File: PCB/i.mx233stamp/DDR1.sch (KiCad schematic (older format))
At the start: 19 parts, among them U2 MT46V32M16TG, U3 M25P32

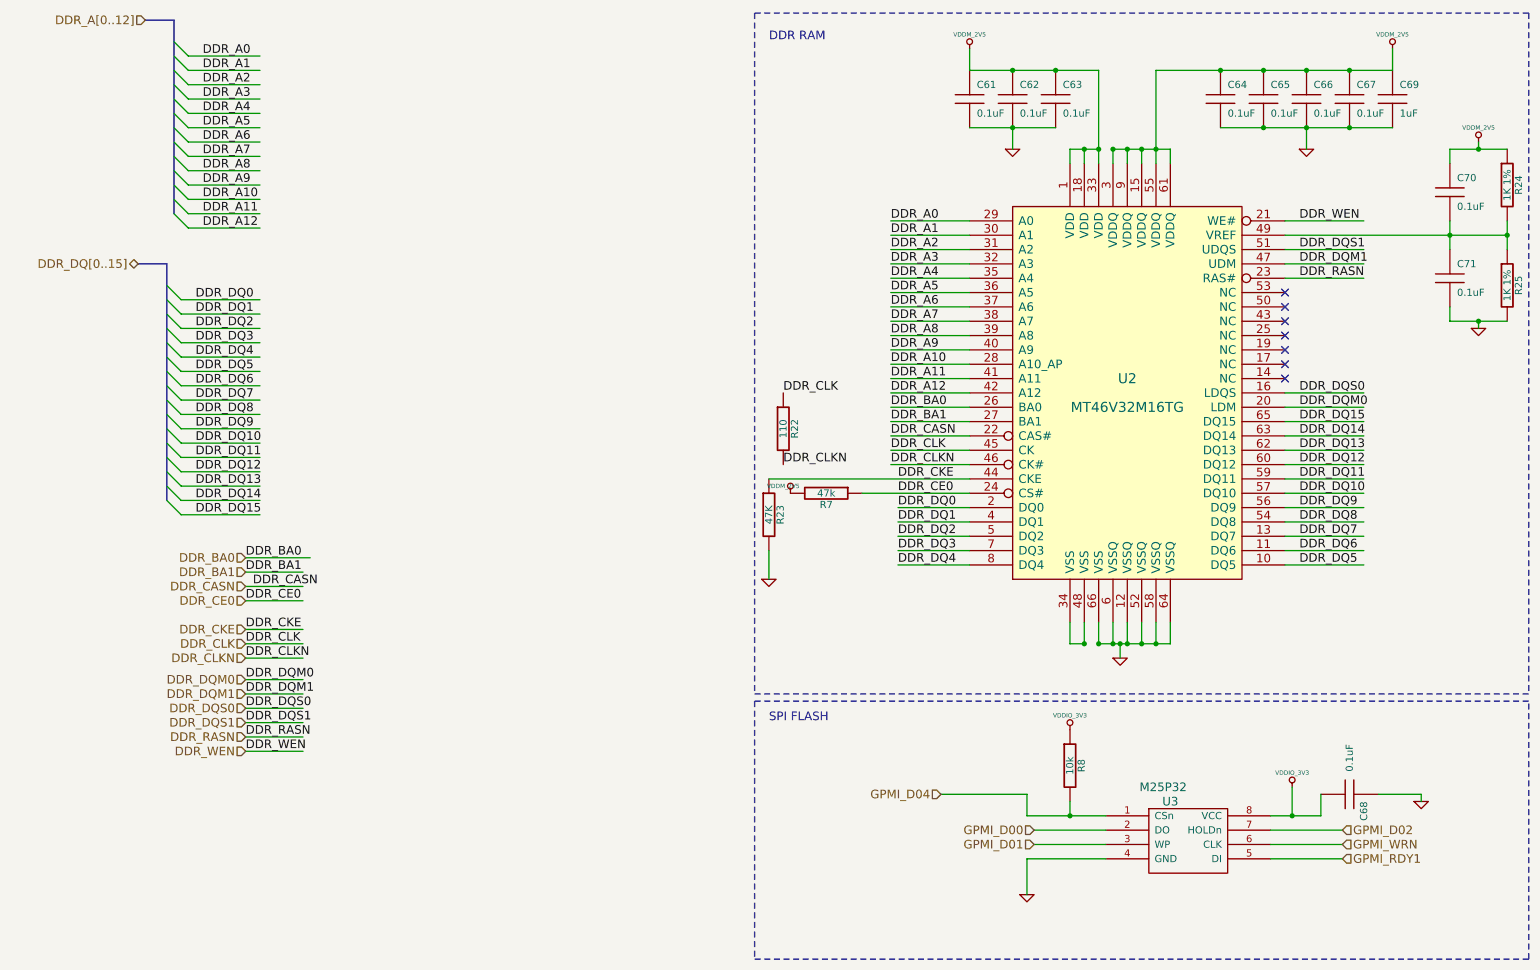
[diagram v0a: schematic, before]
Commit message: Ruteo de la mayoría de las señales de alimentación, corrección del esquemático de la DDR, donde estaban desconectados 2 pines de VSS
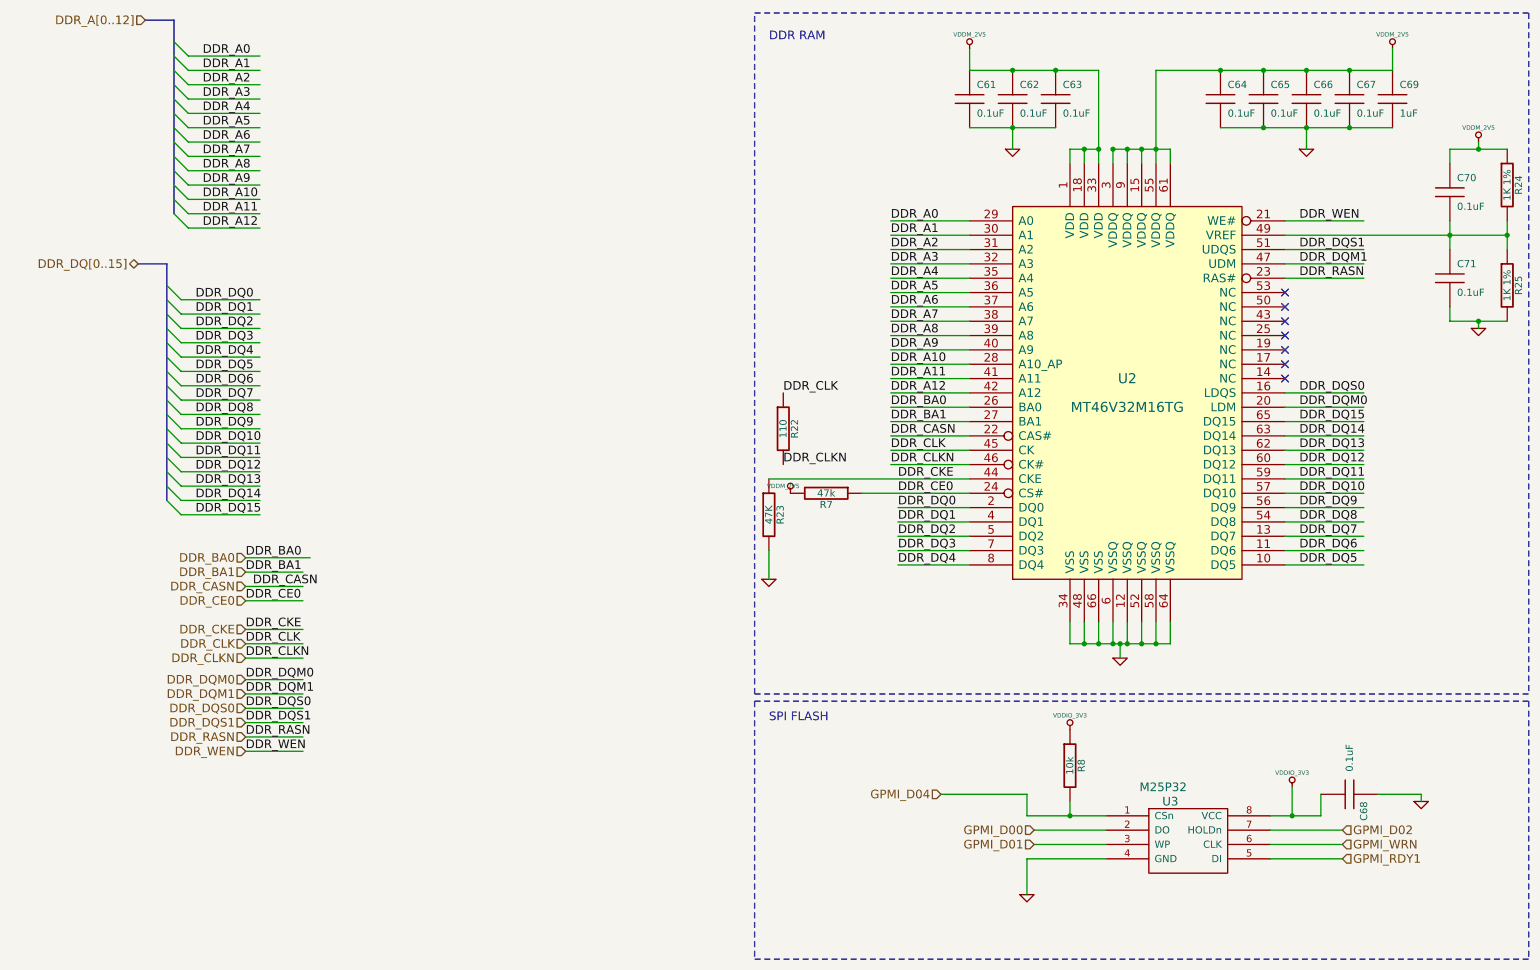
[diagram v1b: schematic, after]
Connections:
- wire segments 139 -> 138
